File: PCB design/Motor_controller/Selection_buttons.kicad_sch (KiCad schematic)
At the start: 18 parts, among them U15 RIC11-31S10K2-GSMT

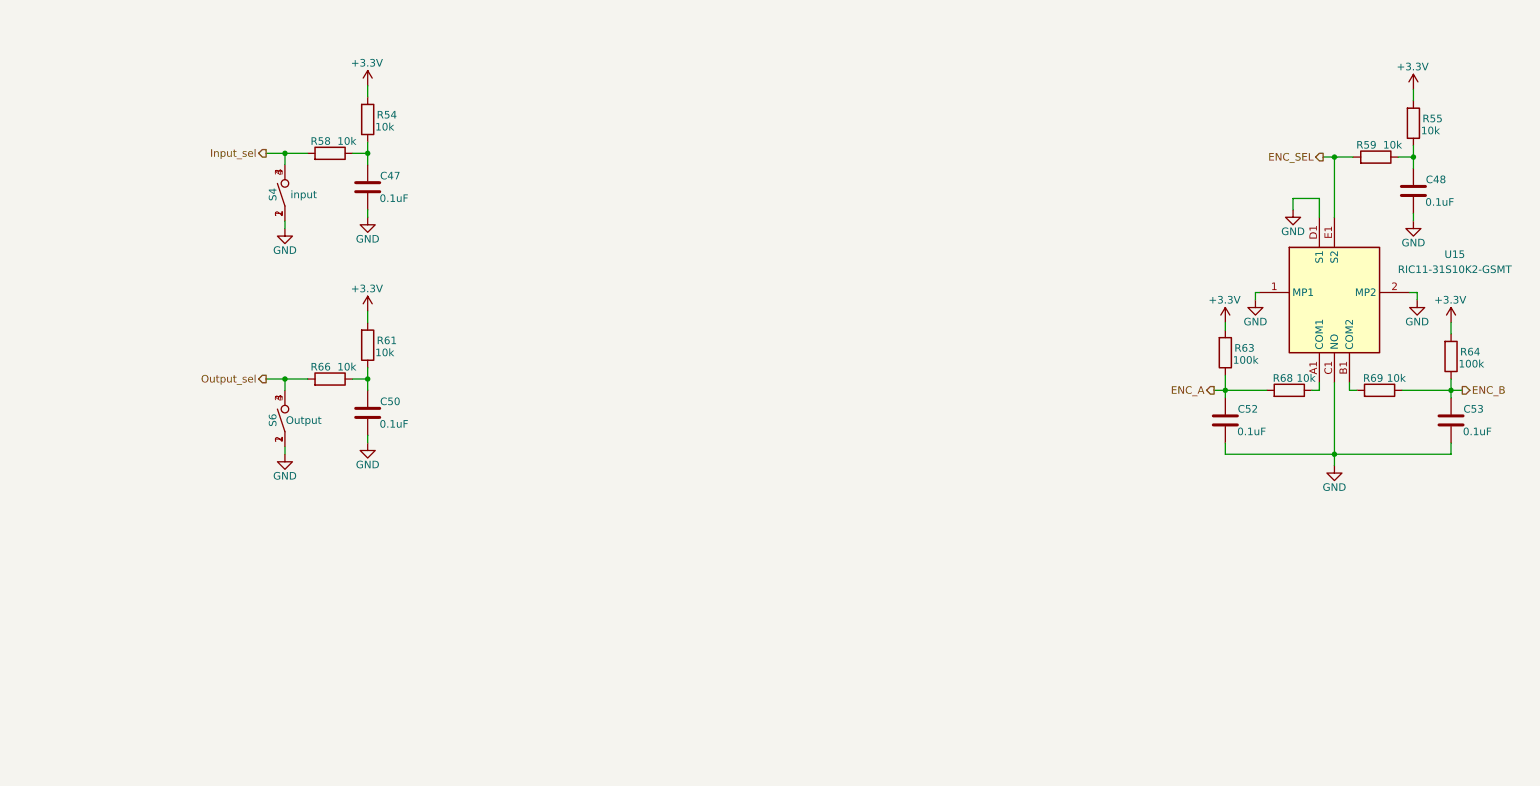
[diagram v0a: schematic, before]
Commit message: Implemented FOC controller
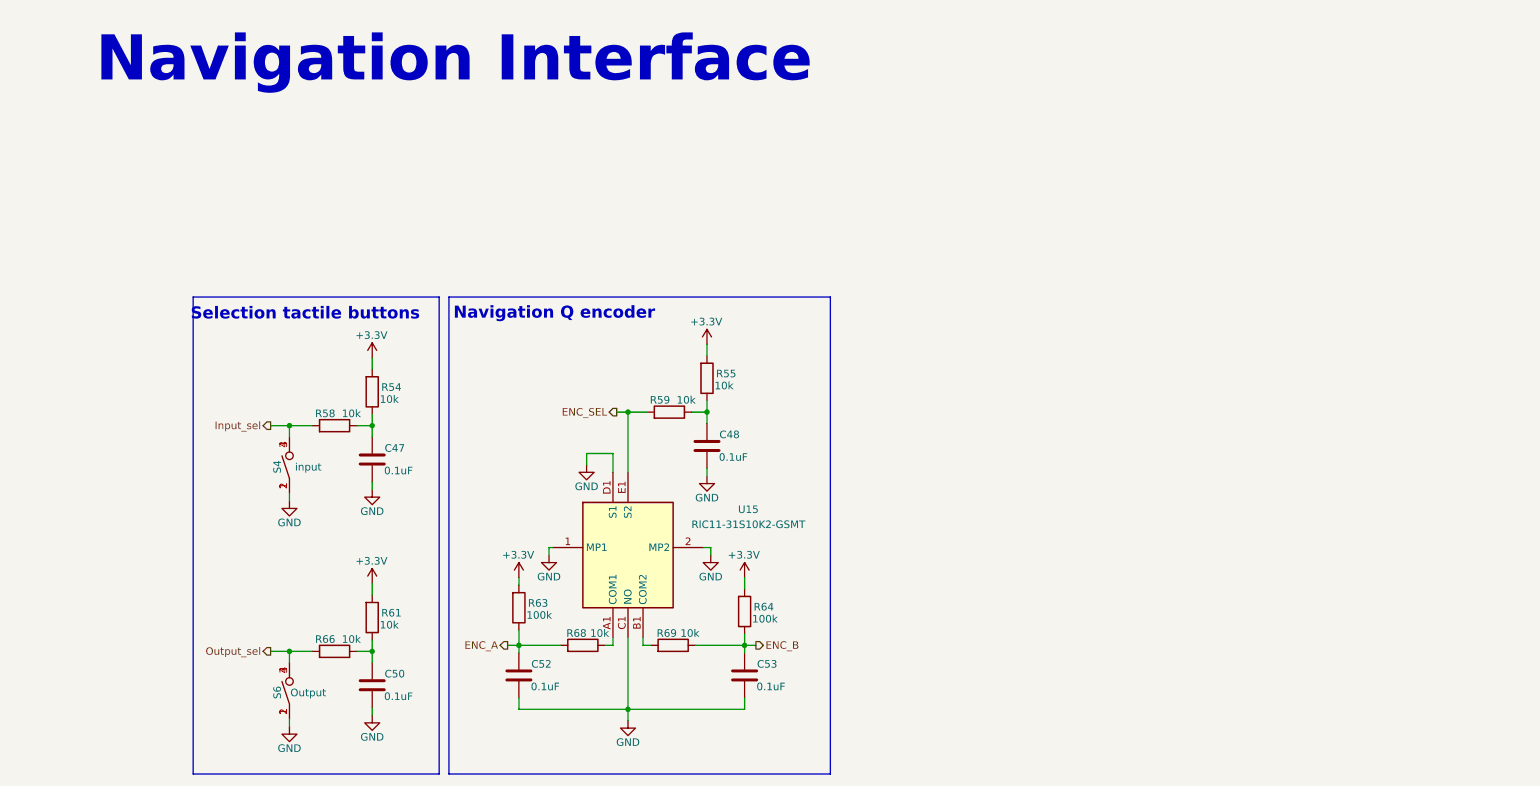
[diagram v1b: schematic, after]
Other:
- note added: "Navigation Interface"
- note added: "Navigation Q encoder"
- note added: "Selection tactile buttons"
- moved on the sheet: C47, C48, C50, C52, C53, R54, R55, R58, R59, R61, R63, R64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
